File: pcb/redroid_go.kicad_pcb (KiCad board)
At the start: 2 copper layers, 70 x 95 mm, 100 parts, among them J1 USB4105-GF-A, J2 5051101892, J3 Conn_01x02_Pin, J4 Conn_01x10_Pin, Q1 UMH3N, Q2 PMOS, Q3 UMH3N, SW1 UP, SW10 A, SW11 SW_SPDT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

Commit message: Add missing GND connectio to ESP32
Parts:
- C17: value 10uF -> 1uF
- C18: value 22uF -> 1uF
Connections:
- U1 pad 15: unconnected-(U1-GND-Pad15) -> GND
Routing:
- net GND: track 72.6 -> 73.8 mm

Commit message: Move charge led
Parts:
- D2: moved to F.Cu
- moved D2 30.9 mm to (160.5, 111.8)
- moved R8 26.4 mm to (161.5, 106.0)
- moved D3 3.01 mm to (166.5, 111.8)
- moved R18 2.06 mm to (165.5, 106.0)
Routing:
- net Net-(D2-K): track 66.1 -> 23.0 mm, vias 3 -> 0
- net VBUS: track 127.1 -> 123.9 mm, vias 3 -> 5
- net Net-(D2-A): track 5.02 -> 2.23 mm
- net IO35: track 94.5 -> 92.9 mm
- net IO2: track 40.8 -> 41.7 mm
- net Net-(D3-A): track 2.05 -> 2.73 mm
- net IO26: track 98.5 -> 97.9 mm
- net GND: vias 37 -> 36

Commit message: Improve LED layout
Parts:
- moved R18 23.5 mm to (172.2, 83.5)
- moved D3 8.43 mm to (162.2, 104.5), turned to 0 degrees
- moved D2 3.04 mm to (163.5, 111.3)
- moved R8 3.00 mm to (158.5, 106.0)
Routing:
- net IO2: track 41.7 -> 14.6 mm, vias 2 -> 0
- net Net-(D3-A): track 2.73 -> 24.6 mm, vias 0 -> 1
- net Net-(D2-A): track 2.23 -> 5.75 mm
- net Net-(D2-K): track 23.0 -> 26.1 mm
- net VBUS: track 123.9 -> 122.1 mm
- net Net-(SW11-B): track 46.9 -> 45.9 mm

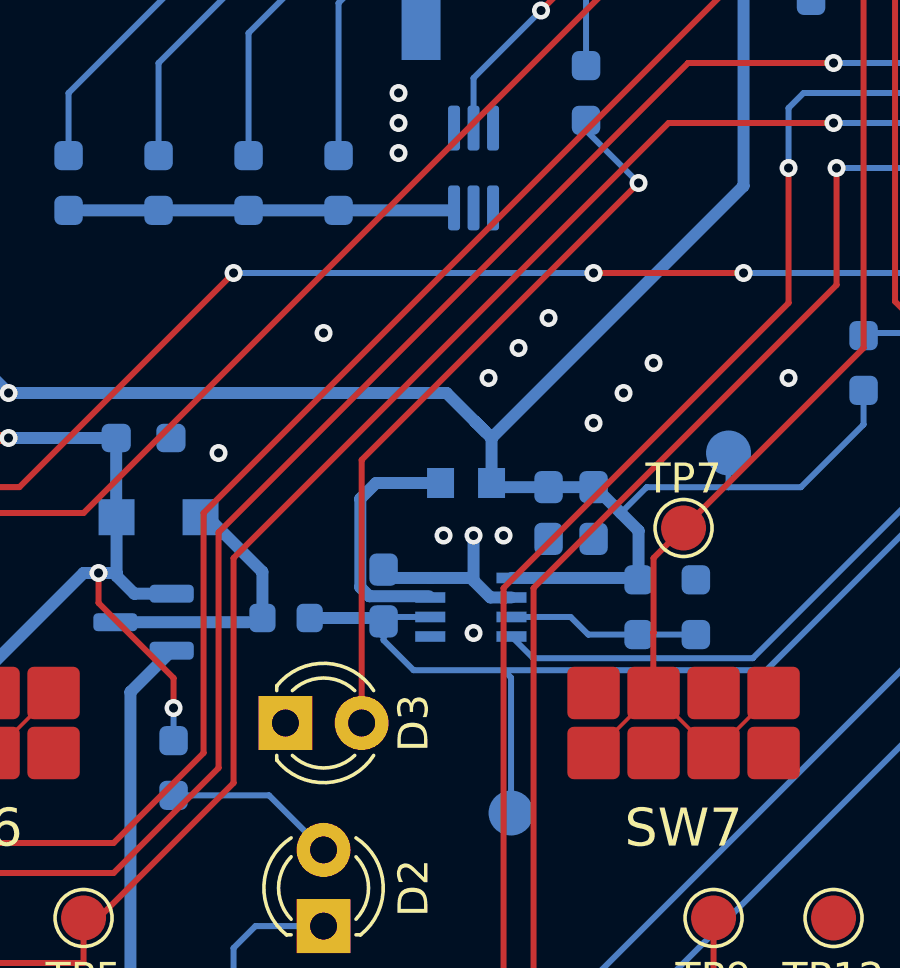
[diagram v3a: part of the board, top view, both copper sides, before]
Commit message: Change led orientation
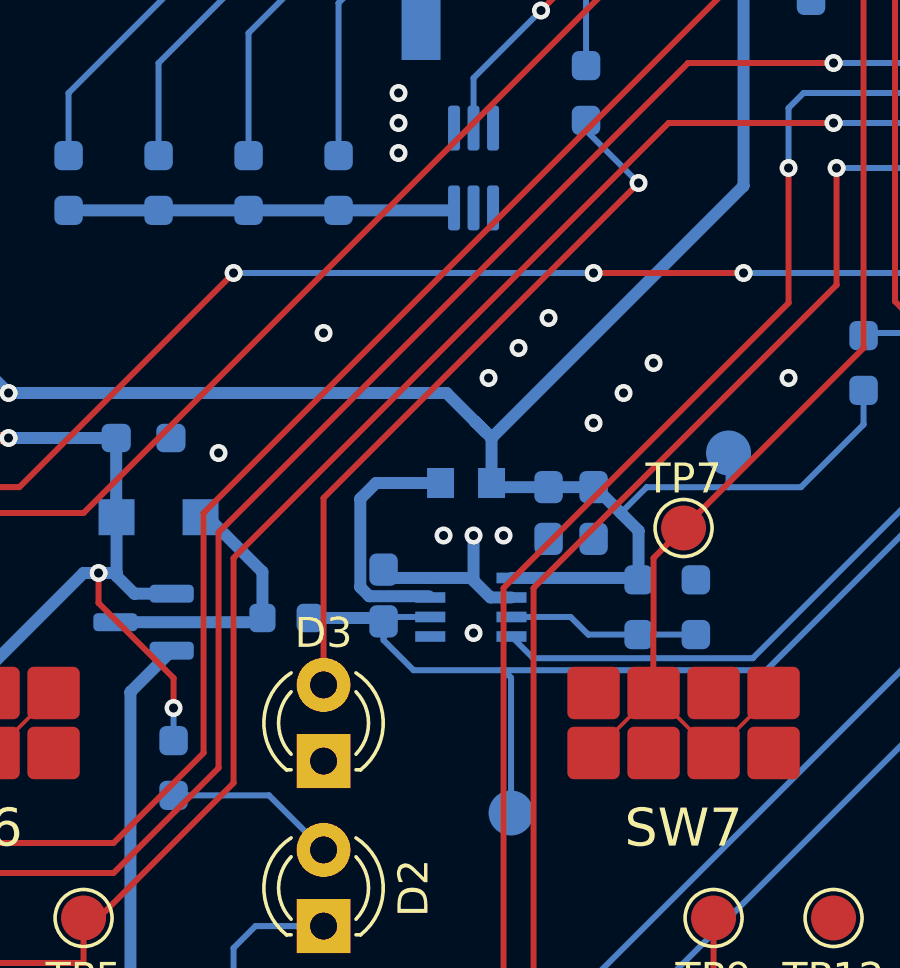
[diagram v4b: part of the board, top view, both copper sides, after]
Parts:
- moved D3 1.80 mm to (163.5, 105.8), turned to 90 degrees
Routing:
- net Net-(D3-A): track 24.6 -> 23.9 mm
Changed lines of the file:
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@@
 	(footprint "LED_THT:LED_D3.0mm"
 		(layer "F.Cu")
-		(at 162.23 104.5)
+		(at 163.5 105.77 90)
 		(descr "LED, diameter 3.0mm, 2 pins, generated by kicad-footprint-generator")
 		(tags "LED")
 		(property "Reference" "D3"
-			(at 4.27 0 90)
+			(at 4.27 0 0)
 			(layer "F.SilkS")
 			(effects
@@
 		)
 		(property "Value" "LED"
-			(at 1.27 2.96 0)
+			(at 1.27 2.96 90)
 			(layer "F.Fab")
 			(effects
@@
 		)
 		(property "Datasheet" "~"
-			(at 0 0 0)
+			(at 0 0 90)
 			(layer "F.Fab")
 			(hide yes)
@@
 		)
 		(property "Description" "Light emitting diode"
-			(at 0 0 0)
+			(at 0 0 90)
 			(layer "F.Fab")
 			(hide yes)
@@
 		)
 		(fp_line
-			(start -1.15 -2.21)
-			(end -1.15 2.21)
+			(start 3.69 -2.21)
+			(end -1.15 -2.21)
 			(stroke
 				(width 0.05)
@@
 		)
 		(fp_line
-			(start -1.15 2.21)
-			(end 3.69 2.21)
+			(start -1.15 -2.21)
+			(end -1.15 2.21)
 			(stroke
 				(width 0.05)
@@
 		)
 		(fp_line
-			(start 3.69 -2.21)
-			(end -1.15 -2.21)
+			(start 3.69 2.21)
+			(end 3.69 -2.21)
 			(stroke
 				(width 0.05)
@@
 		)
 		(fp_line
-			(start 3.69 2.21)
-			(end 3.69 -2.21)
+			(start -1.15 2.21)
+			(end 3.69 2.21)
 			(stroke
 				(width 0.05)
@@
 		)
 		(fp_text user "${REFERENCE}"
-			(at 1.27 0 0)
+			(at 1.27 0 90)
 			(layer "F.Fab")
 			(effects
@@
 		)
 		(pad "1" thru_hole rect
-			(at 0 0)
+			(at 0 0 90)
 			(size 1.8 1.8)
 			(drill 0.9)
@@
 		)
 		(pad "2" thru_hole circle
-			(at 2.54 0)
+			(at 2.54 0 90)
 			(size 1.8 1.8)
 			(drill 0.9)
@@
 	)
 	(segment
-		(start 164.77 104.5)
-		(end 164.77 95.73)
+		(start 163.5 97)
+		(end 174 86.5)
 		(width 0.2)
 		(layer "F.Cu")
@@
 	)
 	(segment
-		(start 164.77 95.73)
-		(end 174 86.5)
+		(start 163.5 103.23)
+		(end 163.5 97)
 		(width 0.2)
 		(layer "F.Cu")

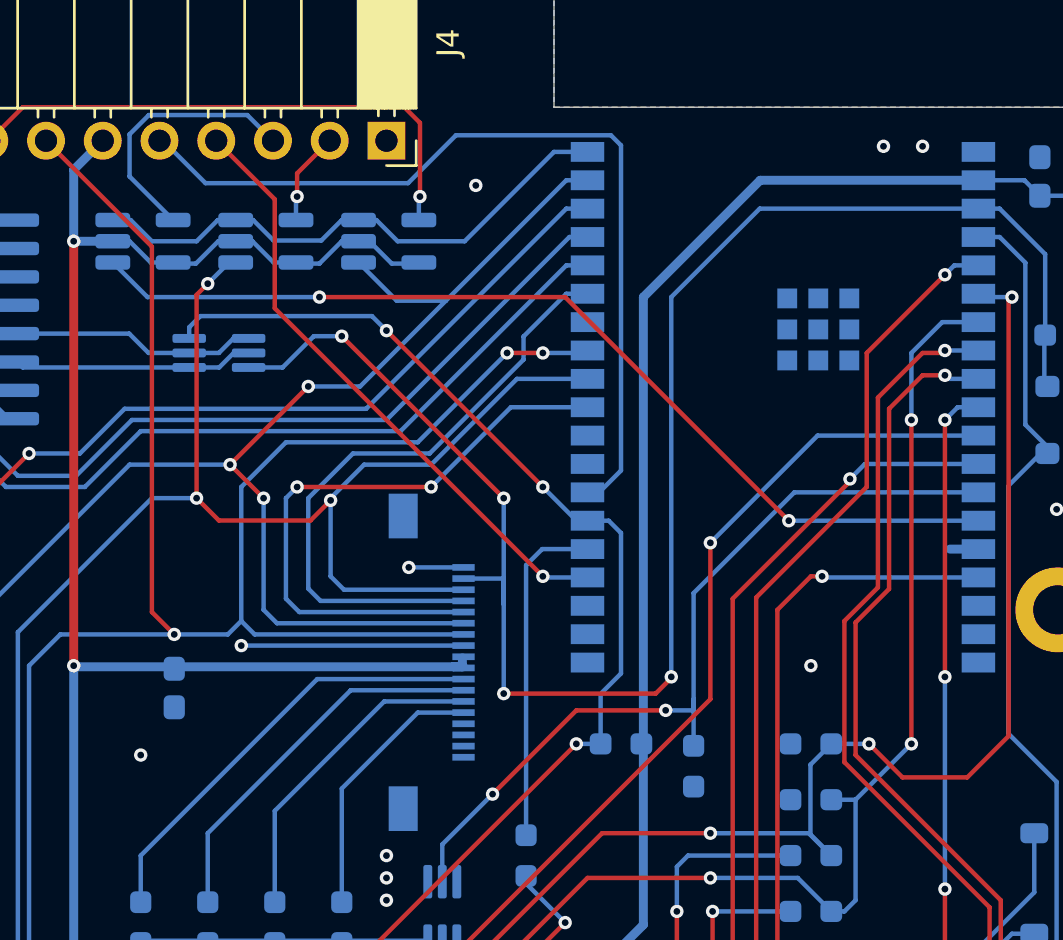
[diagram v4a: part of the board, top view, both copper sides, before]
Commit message: Improvements in vias
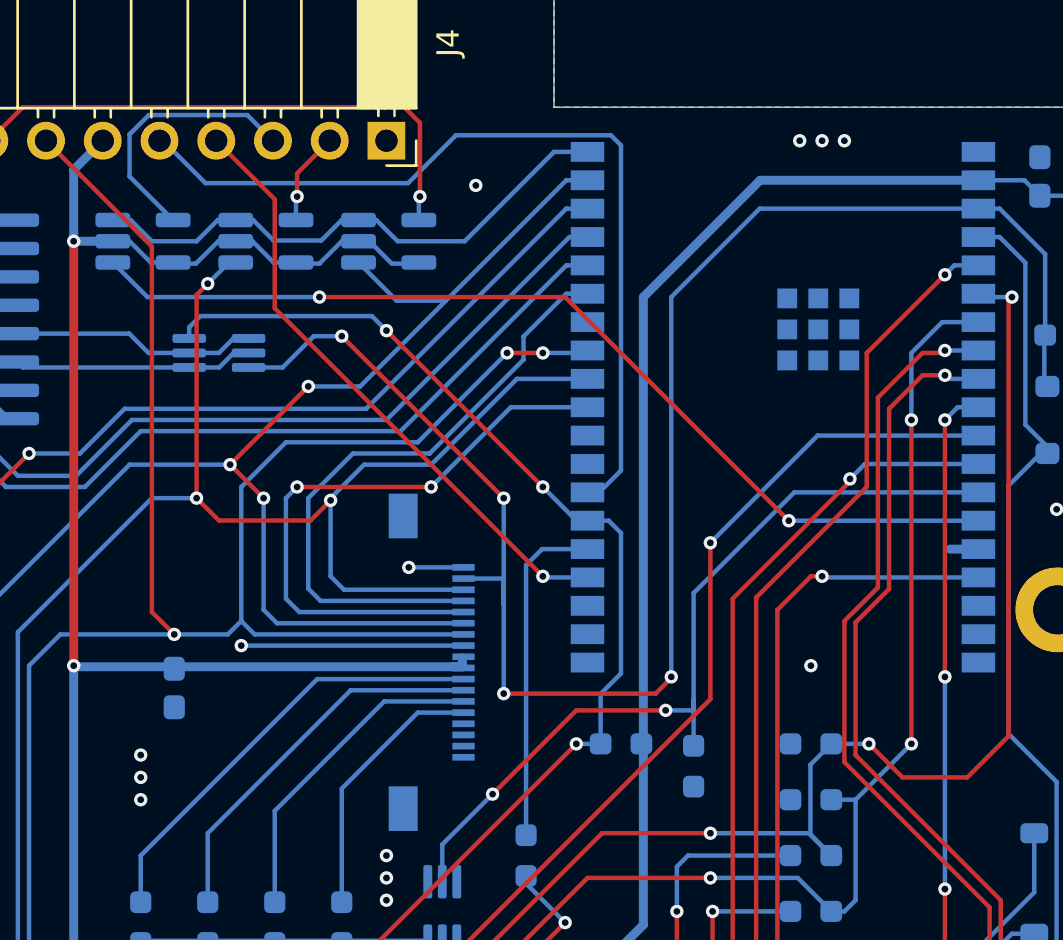
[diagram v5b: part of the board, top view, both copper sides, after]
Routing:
- net GND: vias 36 -> 39
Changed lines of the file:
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@@
+	)
+	(via
+		(at 186.5 51.5)
+		(size 0.6)
+		(drill 0.3)
+		(layers "F.Cu" "B.Cu")
+		(free yes)
+		(net 1)
 	)
 	(via
@@
 	)
 	(via
-		(at 190 51.75)
+		(at 185.5 51.5)
 		(size 0.6)
 		(drill 0.3)
@@
 	)
 	(via
+		(at 155 80)
+		(size 0.6)
+		(drill 0.3)
+		(layers "F.Cu" "B.Cu")
+		(free yes)
+		(net 1)
+	)
+	(via
 		(at 172.5 94.5)
 		(size 0.6)
@@
 	)
 	(via
-		(at 188.25 51.75)
-		(size 0.6)
-		(drill 0.3)
-		(layers "F.Cu" "B.Cu")
-		(free yes)
-		(net 1)
-	)
-	(via
 		(at 138.5 62)
 		(size 0.6)
@@
 	)
 	(via
+		(at 184.5 51.5)
+		(size 0.6)
+		(drill 0.3)
+		(layers "F.Cu" "B.Cu")
+		(free yes)
+		(net 1)
+	)
+	(via
 		(at 167 70.599998)
 		(size 0.6)
@@
 		(size 0.6)
 		(drill 0.3)
+		(layers "F.Cu" "B.Cu")
+		(free yes)
+		(net 1)
+	)
+	(via
+		(at 155 81)
+		(size 0.6)
+		(drill 0.3)

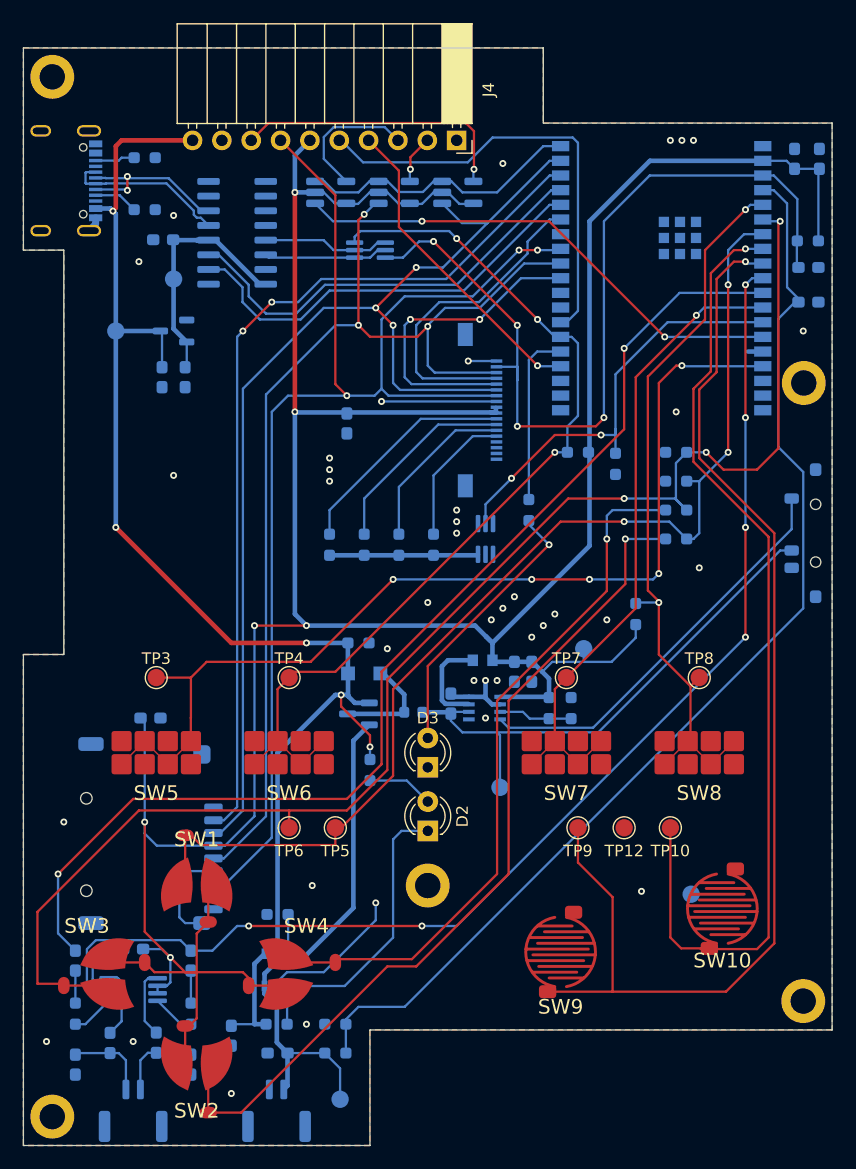
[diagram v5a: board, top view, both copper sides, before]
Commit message: Change pcb for improved power switch
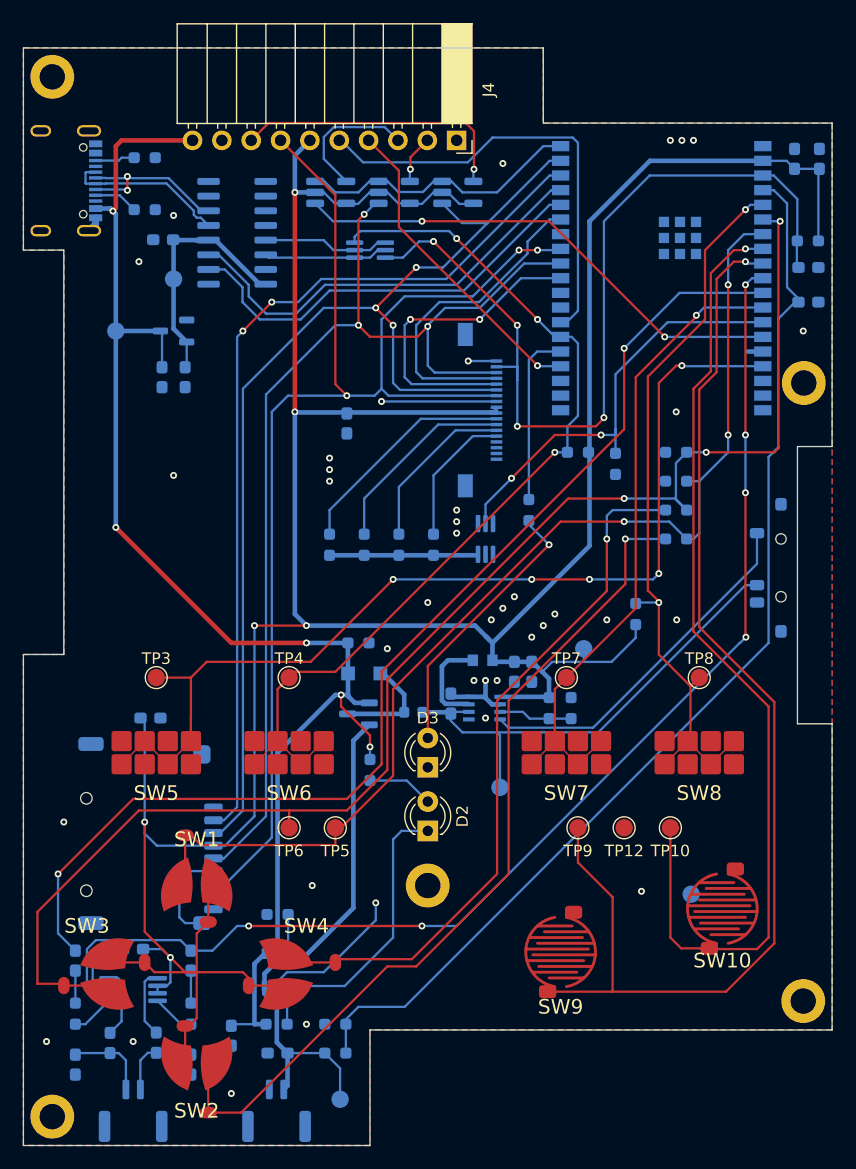
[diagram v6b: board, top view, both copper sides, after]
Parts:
- moved SW11 4.24 mm to (199.5, 85.5)
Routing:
- net Net-(SW11-B): track 45.9 -> 41.7 mm
- net Net-(SW11-A): track 35.3 -> 31.1 mm
- net IO36: track 96.9 -> 95.1 mm
- net IO34: track 121.7 -> 120.4 mm
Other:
- outline, holes or cut-outs redrawn
